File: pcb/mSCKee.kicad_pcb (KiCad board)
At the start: 4 copper layers, 275.3 x 124.4 mm, 192 parts, among them IC1 PCA9956BTWY, IC2 PCA9956BTWY, J2 4P4C, J3 4P4C, J4 USB_C_Receptacle_USB2.0_16P, SW1 SW_Push_45deg, SW10 SW_Push_45deg, SW11 SW_Push_45deg, SW12 SW_Push_45deg, SW13 SW_Push_45deg, SW14 SW_Push_45deg, SW15 SW_Push_45deg, SW16 SW_Push_45deg, SW17 SW_Push_45deg, SW18 SW_Push_45deg, SW19 SW_Push_45deg, SW2 SW_Push_45deg, SW20 SW_Push_45deg, SW21 SW_Push_45deg, SW22 SW_Push_45deg, SW23 SW_Push_45deg, SW24 SW_Push_45deg, SW25 SW_Push_45deg, SW26 SW_Push_45deg, SW27 SW_Push_45deg, SW28 SW_Push_45deg, SW29 SW_Push_45deg, SW3 SW_Push_45deg, SW30 SW_Push_45deg, SW31 SW_Push_45deg, SW32 SW_Push_45deg, SW33 SW_Push_45deg, SW34 SW_Push_45deg, SW35 SW_Push_45deg, SW36 SW_Push_45deg, SW4 SW_Push_45deg, SW5 SW_Push_45deg, SW6 SW_Push_45deg, SW7 SW_Push_45deg, SW8 SW_Push_45deg, SW9 SW_Push_45deg, U1 W25Q128JVSIQ, U2 RP2040, U3 NCP1117LPST33T3G, U4 OPT3001DNPR, U5 NCP1117LPST33T3G, U6 MCP23017T-E/ML, U7 OPT3001DNPR, Y1 ABM8-272-T3

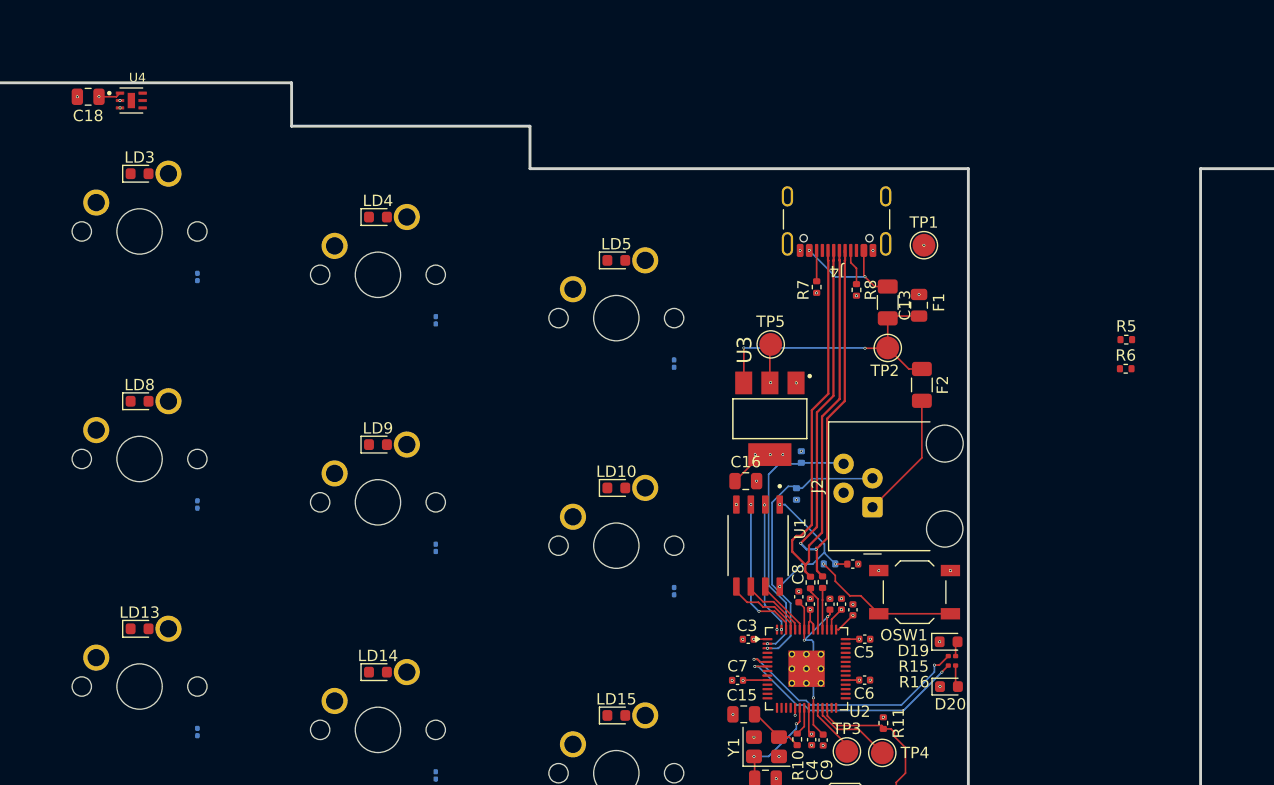
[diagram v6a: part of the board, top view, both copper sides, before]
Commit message: feat: Add I2C left side pullups, move status LED resistors to backside
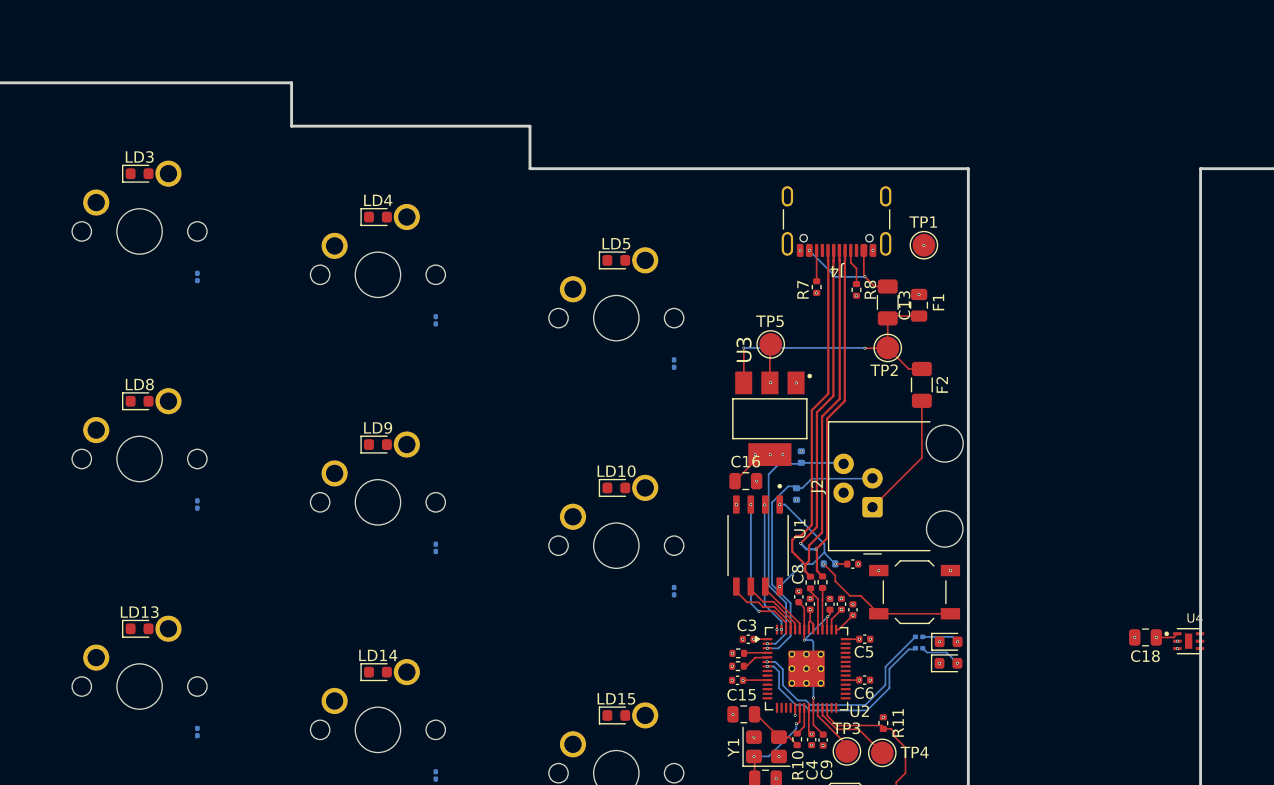
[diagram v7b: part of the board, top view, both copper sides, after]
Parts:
- R15, R16: moved to B.Cu
- moved C18 104.4 mm to (214.2, 115.7)
- moved U4 104.4 mm to (218.0, 116.0)
- moved R5 43.9 mm to (178.4, 117.1)
- moved R6 43.0 mm to (178.3, 118.2)
- moved R15 3.35 mm to (194.3, 115.7)
- moved R16 3.27 mm to (194.3, 116.7)
- moved D20 2.05 mm to (196.8, 118.0)
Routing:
- net STATUS1: track 22.2 -> 18.9 mm, vias 2 -> 1
- net STATUS2: track 21.4 -> 18.7 mm, vias 2 -> 1
- net I2C_CLK: track 0.00 -> 2.40 mm
- net Net-(D19-A): track 1.33 -> 3.48 mm, vias 0 -> 1
- net I2C_D: track 0.00 -> 2.08 mm
- net Net-(D20-A): track 1.93 -> 3.60 mm, vias 0 -> 1
- net +3V3: vias 20 -> 22

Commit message: feat: Route switches amongst themselves & Remove weirdly behaving netclass sizes
TODO: route LD's and figure out how to connect them all to the driver (put driver IC on back side of board?)
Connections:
- D16 pad 1: ROW2 -> ROW0
- D17 pad 1: ROW2 -> ROW1
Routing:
- net ROW1: track 0.00 -> 93.7 mm
- net ROW0: track 0.00 -> 93.7 mm
- net ROW2: track 0.00 -> 93.7 mm
- net COL6: track 0.00 -> 56.7 mm
- net COL8: track 0.00 -> 40.0 mm
- net COL3: track 0.00 -> 40.0 mm
- net COL9: track 0.00 -> 40.0 mm
- net COL7: track 0.00 -> 40.0 mm
- net COL4: track 0.00 -> 40.0 mm
- net COL2: track 0.00 -> 40.0 mm
- net COL11: track 0.00 -> 40.0 mm
- net COL10: track 0.00 -> 40.0 mm
- net COL1: track 0.00 -> 40.0 mm
- net COL0: track 0.00 -> 40.0 mm
- net Net-(D35-A): track 0.00 -> 9.86 mm
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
